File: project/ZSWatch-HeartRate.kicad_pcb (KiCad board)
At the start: 2 copper layers, 27.5 x 18.2 mm, 19 parts, among them IC101 MAX32664, IC102 MAXM86161, X101 Mainboard, Y101 32kHz

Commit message: - Working on version 1
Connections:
- net /V_Bat renamed /V_LED
- IC101 pad 1: unconnected-(IC101-MFIO-Pad1) -> /MFIO
- X101 pad 1: /INT_ACC -> /INT_HR
- X101 pad 3: unconnected-(X101-Pin_3-Pad3) -> /INT_ACC
- X101 pad 7: unconnected-(X101-Pin_7-Pad7) -> /SDA
- X101 pad 9: /SDA -> /MFIO
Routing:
- net /MFIO: track 0.00 -> 12.4 mm, vias 0 -> 1
- net /INT_HR: track 12.9 -> 23.1 mm

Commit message: First dev board version
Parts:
- removed G*** (x2): LOGO, LOGO
- removed X101: Mainboard, Amphenol:101R014FB110
- added C108: 4u7, Capacitor_SMD:C_0603_1608Metric, F.Cu at (163.2, 103.4)
- added C109: 100n, Capacitor_SMD:C_0603_1608Metric, F.Cu at (154.8, 116.3)
- added C110: 1u, Capacitor_SMD:C_0603_1608Metric, F.Cu at (162.6, 94.3)
- added C111: 1u, Capacitor_SMD:C_0402_1005Metric, F.Cu at (166.0, 110.2)
- added C112: 1u, Capacitor_SMD:C_0402_1005Metric, F.Cu at (164.1, 108.8)
- added C113: 1u, Capacitor_SMD:C_0603_1608Metric, F.Cu at (161.9, 99.3)
- added C114: 100n, Capacitor_SMD:C_0402_1005Metric, B.Cu at (169.1, 109.3)
- added C115: 10u, Capacitor_SMD:C_0402_1005Metric, B.Cu at (170.1, 109.3)
- added C116: 100n, Capacitor_SMD:C_0402_1005Metric, B.Cu at (168.1, 109.3)
- added D102: D_Photo, Vishay:VEMD5080X01, B.Cu at (166.2, 101.0)
- added D104: RED, Diode_SMD:D_0603_1608Metric, B.Cu at (170.7, 101.0)
- added D105: IR, Diode_SMD:D_0603_1608Metric, B.Cu at (161.7, 101.0)
- added D106: GREEN, Diode_SMD:D_0603_1608Metric, B.Cu at (166.2, 104.8)
- added D107: STATUS, LED_SMD:LED_0805_2012Metric_Pad1.15x1.40mm_HandSolder, F.Cu at (155.6, 103.4)
- added IC103: MAX32664, Package_BGA_Kampi:WLP-16_2x2mm_P0.5mm, F.Cu at (166.2, 108.1)
- added IC104: TPS61240, Package_BGA_Kampi:DSBGA-6_0.886x1.288mm_2x3_P0.4mm, F.Cu at (161.7, 104.4)
- added IC105: MAX86141, Package_BGA_Kampi:THIN-WLP-20_2.228x1.967mm_P0.4mm, F.Cu at (166.2, 101.0)
- added IC106: MIC5365-1.8, Package_TO_SOT_SMD:SOT-23-5, F.Cu at (162.3, 96.8)
- added J101: SPI, Connector_PinHeader_2.54mm:PinHeader_1x06_P2.54mm_Vertical, F.Cu at (169.9, 89.8)
- added J102: GPIO, Connector_PinHeader_2.54mm:PinHeader_1x07_P2.54mm_Vertical, F.Cu at (174.5, 116.0)
- added J103: UART, Connector_PinHeader_2.54mm:PinHeader_1x03_P2.54mm_Vertical, F.Cu at (148.2, 103.0)
- added J104: I2C, Connector_PinHeader_2.54mm:PinHeader_1x03_P2.54mm_Vertical, F.Cu at (184.2, 110.8)
- added L101: 1u, Inductor_SMD:L_0603_1608Metric, F.Cu at (160.7, 105.7)
- added M101: BM15C, Fanstel:BM15C, F.Cu at (148.2, 110.5)
- added R107: 10k, Capacitor_SMD:C_0603_1608Metric, F.Cu at (157.7, 99.5)
- added R108: 10k, Capacitor_SMD:C_0603_1608Metric, B.Cu at (157.8, 109.8)
- added R109: 0R, Resistor_SMD:R_0805_2012Metric, F.Cu at (153.6, 103.6)
- added SW101: BTN1, Wuerth:WS-TASV-6x6, F.Cu at (176.3, 98.7)
- added SW102: RESET, Wuerth:WS-TASV-6x6, F.Cu at (176.3, 108.9)
- added X102: CHARGE, Connector_USB:USB_C_Receptacle_GCT_USB4105-xx-A_16P_TopMnt_Horizontal, F.Cu at (144.8, 95.4)
- added X103: BATTERY, Molex:78171-0002, F.Cu at (157.0, 90.5)
- added X104: DEBUG, Connector_PinHeader_1.27mm:PinHeader_2x05_P1.27mm_Vertical, F.Cu at (166.7, 89.6)
- C101: value 100n -> 4u7; footprint Capacitor_SMD:C_0603_1608Metric_Pad1.08x0.95mm_HandSolder -> Capacitor_SMD:C_0603_1608Metric; moved to F.Cu
- C102: value 1u -> 4u7; footprint Capacitor_SMD:C_0603_1608Metric_Pad1.08x0.95mm_HandSolder -> Capacitor_SMD:C_0603_1608Metric; moved to F.Cu
- C103: value 1u -> 100n; footprint Capacitor_SMD:C_0603_1608Metric_Pad1.08x0.95mm_HandSolder -> Capacitor_SMD:C_0402_1005Metric; moved to F.Cu
- C104: footprint Capacitor_SMD:C_0603_1608Metric_Pad1.08x0.95mm_HandSolder -> Capacitor_SMD:C_0402_1005Metric; moved to F.Cu
- C105: value 1u -> 22u; footprint Capacitor_SMD:C_0603_1608Metric_Pad1.08x0.95mm_HandSolder -> Capacitor_SMD:C_0402_1005Metric; moved to F.Cu
- C106: value 1u -> 10u; footprint Capacitor_SMD:C_0603_1608Metric_Pad1.08x0.95mm_HandSolder -> Capacitor_SMD:C_0402_1005Metric; moved to F.Cu
- C107: value 1u -> 2u2; footprint Capacitor_SMD:C_0603_1608Metric_Pad1.08x0.95mm_HandSolder -> Capacitor_SMD:C_0603_1608Metric; moved to F.Cu
- IC101: value MAX32664 -> LIS2DS12; footprint Package_DFN_QFN:QFN-24-1EP_3x3mm_P0.4mm_EP1.75x1.6mm -> Package_LGA:LGA-12_2x2mm_P0.5mm
- IC102: value MAXM86161 -> MCP73832-2-OT; footprint AnalogDevices:MAXM86161 -> Package_TO_SOT_SMD:SOT-23-5; moved to F.Cu
- R101: value 10R -> 10k; footprint Resistor_SMD:R_0603_1608Metric_Pad0.98x0.95mm_HandSolder -> Capacitor_SMD:C_0603_1608Metric; moved to F.Cu
- R102, R104: value 4k7 -> 5k1; footprint Resistor_SMD:R_0603_1608Metric_Pad0.98x0.95mm_HandSolder -> Resistor_SMD:R_0603_1608Metric; moved to F.Cu
- R103: footprint Resistor_SMD:R_0603_1608Metric_Pad0.98x0.95mm_HandSolder -> Resistor_SMD:R_0402_1005Metric; moved to F.Cu
- R105: value 4k7 -> 220R; footprint Resistor_SMD:R_0603_1608Metric_Pad0.98x0.95mm_HandSolder -> Capacitor_SMD:C_0603_1608Metric; moved to F.Cu
- R106: value 4k7 -> 10k; footprint Resistor_SMD:R_0603_1608Metric_Pad0.98x0.95mm_HandSolder -> Capacitor_SMD:C_0603_1608Metric; moved to F.Cu
- Y101: footprint Crystal:Crystal_SMD_3215-2Pin_3.2x1.5mm -> Crystal_Kampi:ECS_ECX-1210; moved to F.Cu
- moved R102 40.0 mm to (151.2, 94.2), turned to 0 degrees
- moved C101 31.5 mm to (155.4, 94.3), turned to 180 degrees
- moved R106 29.6 mm to (154.5, 97.0), turned to 90 degrees
- moved R104 29.0 mm to (151.2, 97.2), turned to 180 degrees
- moved R105 24.8 mm to (157.4, 103.2), turned to 90 degrees
- moved C102 24.0 mm to (158.4, 94.3), turned to 0 degrees
- moved IC102 22.8 mm to (157.3, 96.8), turned to 180 degrees
- moved C103 22.8 mm to (166.4, 99.2), turned to 180 degrees
- moved R103 22.2 mm to (164.1, 107.8), turned to 0 degrees
- moved C107 18.6 mm to (160.1, 103.4), turned to 90 degrees
- moved C104 15.3 mm to (164.0, 101.2)
- moved R101 13.6 mm to (168.9, 108.3), turned to 0 degrees
- moved IC101 12.5 mm to (168.8, 107.1), turned to -90 degrees
- moved C105 11.3 mm to (166.4, 98.2), turned to 180 degrees
- moved Y101 10.0 mm to (167.4, 110.0), turned to 180 degrees
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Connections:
- C101 pad 1: /~{RESET} -> Net-(IC102-V_{DD})
- C101 pad 2: Net-(C101-Pad2) -> GND
- C102 pad 1: +1V8 -> /V_{BAT}
- C104 pad 1: Net-(IC101-VCore) -> Net-(IC105-VREF)
- C105 pad 1: /V_LED -> +1V8
- C106 pad 1: Net-(IC102-VREF) -> /V_{LED}
- C107 pad 1: Net-(IC102-VLDO) -> /V_{BAT}
- IC101 pad 1: /MFIO -> Net-(IC101-SCL/SCLK)
- IC101 pad 10: GND -> +1V8
- IC101 pad 11: +1V8 -> unconnected-(IC101-INT2-Pad11)
- IC101 pad 12: Net-(IC101-VCore) -> /INT_{ACC}
- IC101 pad 2: (no net) -> Net-(IC101-CS)
- IC101 pad 3: (no net) -> Net-(IC101-SDO/ADDR0)
- IC101 pad 4: (no net) -> Net-(IC101-SDA/SDI/SDO)
- IC101 pad 5: (no net) -> unconnected-(IC101-NC-Pad5)
- IC101 pad 6: /~{RESET} -> GND
- IC101 pad 8: Net-(IC101-32KOUT) -> GND
- IC101 pad 9: Net-(IC101-32KIN) -> +1V8
- IC102 pad 1: Net-(IC101-SDA_Sensor) -> /CHARGE
- IC102 pad 2: Net-(IC101-SCL_Sensor) -> GND
- IC102 pad 3: Net-(IC101-LDO_EN) -> /V_{BAT}
- IC102 pad 4: Net-(IC102-VLDO) -> Net-(IC102-V_{DD})
- IC102 pad 5: /V_LED -> Net-(IC102-PROG)
- R101 pad 1: GND -> /~{RESET_{HR}}
- R101 pad 2: Net-(C101-Pad2) -> GND
- R102 pad 1: +1V8 -> Net-(X102-CC1)
- R102 pad 2: /SCL -> GND
- R103 pad 2: /SDA -> Net-(IC103-INT_{PPG})
- R104 pad 1: +1V8 -> GND
- R104 pad 2: Net-(IC101-SDA_Sensor) -> Net-(X102-CC2)
- R105 pad 1: +1V8 -> +BATT
- R105 pad 2: Net-(IC101-SCL_Sensor) -> Net-(D107-A)
- R106 pad 1: +1V8 -> Net-(IC102-PROG)
- R106 pad 2: /INT_HR -> GND
- Y101 pad 1: Net-(IC101-32KIN) -> Net-(IC103-32k_{OUT})
- Y101 pad 2: Net-(IC101-32KOUT) -> Net-(IC103-32k_{IN})
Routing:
- net GND: track 1.17 -> 60.5 mm, vias 1 -> 29
- net /~{RESET}: track 14.3 -> 57.3 mm, vias 1 -> 2
- net Net-(M101-P2.03): track 0.00 -> 37.3 mm, vias 0 -> 2
- net Net-(IC103-CS_{PPG}): track 0.00 -> 32.3 mm, vias 0 -> 1
- net Net-(IC101-SDO/ADDR0): track 0.00 -> 30.0 mm, vias 0 -> 2
- net Net-(IC101-SDA/SDI/SDO): track 0.00 -> 28.9 mm, vias 0 -> 1
- net Net-(IC101-CS): track 0.00 -> 28.1 mm, vias 0 -> 2
- net Net-(IC101-SCL/SCLK): track 0.00 -> 26.8 mm, vias 0 -> 3
- net /SWDIO: track 0.00 -> 26.1 mm, vias 0 -> 1
- net Net-(J102-Pin_2): track 0.00 -> 25.3 mm, vias 0 -> 1
- net Net-(J102-Pin_4): track 0.00 -> 24.4 mm, vias 0 -> 1
- net /SWDCLK: track 0.00 -> 24.2 mm, vias 0 -> 1
- net /INT_HR: track 23.1 -> 0.00 mm, vias 2 -> 0
- net Net-(J102-Pin_3): track 0.00 -> 21.8 mm, vias 0 -> 2
- net /V_{BAT}: track 0.00 -> 19.7 mm
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- added copper zone on In1.Cu, net (none)
- added copper zone on In2.Cu, net +1V8
- added copper zone on In2.Cu, net /V_{LED}
- added copper zone on In1.Cu, net GND
- added copper zone on F.Cu, net Net-(IC102-V_{DD})
- removed copper zone on F.Cu, net +1V8
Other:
- board size 27.5 x 18.2 mm -> 45 x 36.9 mm
- copper layers 2 -> 4
- board text removed: "0.0.${REVISION}"

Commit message: Update CI/CD pipeline
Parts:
- added C117: 1u, Capacitor_SMD:C_0402_1005Metric, F.Cu at (172.1, 108.0)
- C109: footprint Capacitor_SMD:C_0603_1608Metric -> Capacitor_SMD:C_0402_1005Metric
- D104: value RED -> IR
- D105: value IR -> GREEN
- D106: value GREEN -> RED
- IC103: footprint Package_BGA_Kampi:WLP-16_2x2mm_P0.5mm -> Package_DFN_QFN:QFN-24-1EP_3x3mm_P0.4mm_EP1.75x1.6mm
- J104: footprint Connector_PinHeader_2.54mm:PinHeader_1x03_P2.54mm_Vertical -> Connector_PinHeader_2.54mm:PinHeader_1x04_P2.54mm_Vertical
- R101, R106, R107: footprint Capacitor_SMD:C_0603_1608Metric -> Resistor_SMD:R_0402_1005Metric
- R102, R104: footprint Resistor_SMD:R_0603_1608Metric -> Resistor_SMD:R_0402_1005Metric
- R108: footprint Capacitor_SMD:C_0603_1608Metric -> Resistor_SMD:R_0402_1005Metric; moved to F.Cu
- moved R108 8.86 mm to (151.6, 116.0), turned to 180 degrees
- moved C115 8.67 mm to (161.4, 109.1), turned to 180 degrees
- moved C112 8.18 mm to (172.1, 107.0), turned to 0 degrees
- moved C114 7.78 mm to (161.4, 108.1), turned to 180 degrees
- moved C116 7.04 mm to (161.4, 107.0), turned to 180 degrees
- moved R103 5.80 mm to (169.5, 105.8), turned to -90 degrees
- moved IC101 5.20 mm to (163.7, 107.8), turned to 180 degrees
- moved Y101 4.36 mm to (171.8, 109.8), turned to 90 degrees
- moved R101 3.70 mm to (170.5, 111.7)
- moved IC103 2.83 mm to (168.9, 109.0), turned to 90 degrees
- moved J104 2.54 mm to (184.2, 108.3)
- moved C111 0.88 mm to (165.5, 109.5), turned to 180 degrees
- moved C109 0.48 mm to (155.2, 116.0)
- turned SW101 to -90 degrees
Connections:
- J101 pad 2: Net-(IC101-SCL/SCLK) -> Net-(IC101-SDA/SDI/SDO)
- J101 pad 3: Net-(IC101-SDA/SDI/SDO) -> Net-(IC101-SDO/ADDR0)
- J101 pad 4: Net-(IC101-SDO/ADDR0) -> Net-(IC101-SCL/SCLK)
- J104 pad 3: GND -> /~{RESET_{HR}}
- SW101 pad 2: GND -> Net-(M101-P2.03)
- SW101 pad 3: Net-(M101-P2.03) -> GND
- SW102 pad 2: /~{RESET} -> GND
- SW102 pad 3: GND -> /~{RESET}
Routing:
- net /~{RESET_{HR}}: track 17.2 -> 31.7 mm
- net Net-(IC101-CS): track 28.1 -> 39.6 mm, vias 2 -> 3
- net /~{RESET}: track 57.3 -> 68.5 mm, vias 2 -> 3
- net /SCL: track 34.3 -> 43.3 mm
- net GND: track 60.5 -> 67.6 mm, vias 29 -> 31
- net Net-(IC101-SCL/SCLK): track 26.8 -> 31.2 mm
- net /INT_{ACC}: track 3.93 -> 8.05 mm, vias 1 -> 2
- net Net-(J102-Pin_3): track 21.8 -> 25.4 mm
- net Net-(M101-P2.03): track 37.3 -> 40.7 mm
- net /SDA: track 35.1 -> 38.4 mm
- net +1V8: track 18.2 -> 20.6 mm, vias 8 -> 9
- net Net-(IC101-SDO/ADDR0): track 30.0 -> 31.2 mm
- net Net-(IC103-V_{CORE}): track 0.92 -> 1.82 mm
- net Net-(IC103-INT_{PPG}): track 9.05 -> 8.44 mm
- net Net-(IC103-CS_{PPG}): track 32.3 -> 31.7 mm
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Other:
- board text added: "${REVISION}"

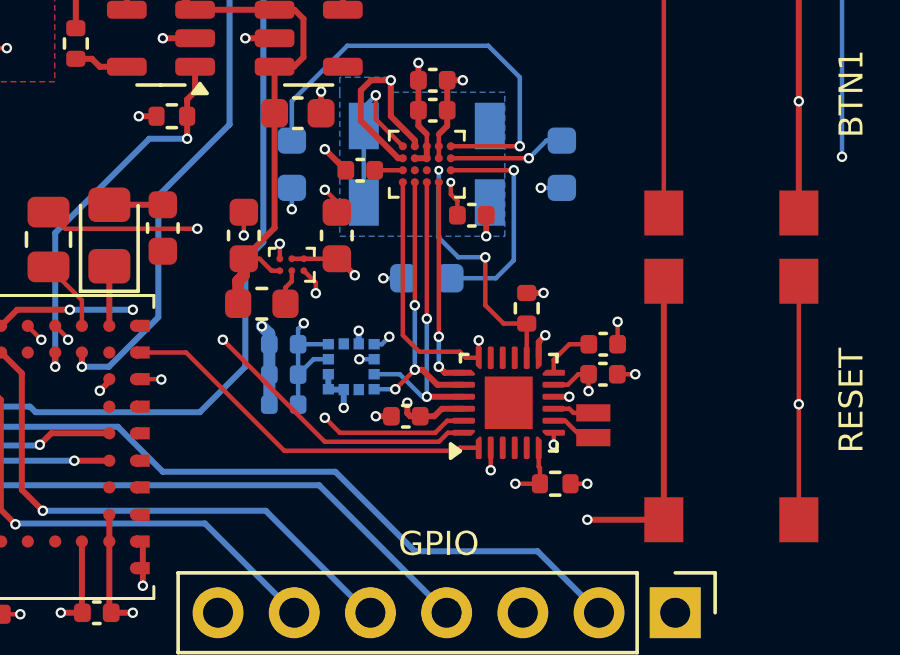
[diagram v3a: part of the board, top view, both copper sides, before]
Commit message: Fix wrong MAX32664 footprint
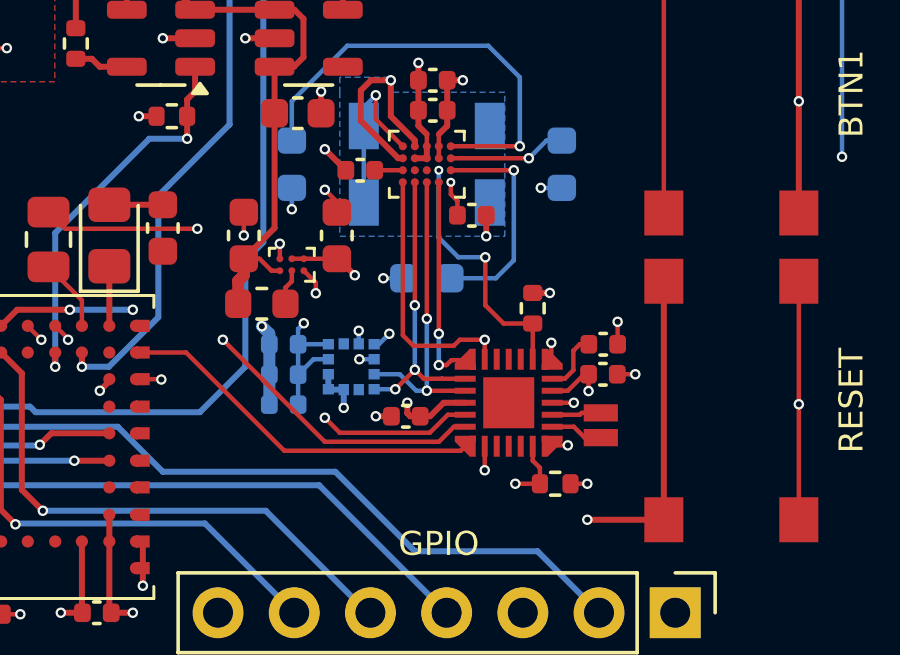
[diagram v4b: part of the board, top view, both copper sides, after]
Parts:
- IC103: footprint Package_DFN_QFN:QFN-24-1EP_3x3mm_P0.4mm_EP1.75x1.6mm -> Analog Devices:MAX32664GTG
- moved Y101 0.25 mm to (172.0, 109.8)
- moved R103 0.20 mm to (169.7, 105.8)
